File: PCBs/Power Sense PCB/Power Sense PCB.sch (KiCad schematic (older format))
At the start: 0 parts

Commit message: Complete Schematic
- Completed initial schematic
- Lots of test points
- Some footprints and BOM selected
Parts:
- added C1, C10, C11, C12, C2, C3, C4, C5, C6, C7, C8, C9: C_Small, Capacitors_SMD:C_0603, symbol Device:C_Small
- added H1, H2, H3, H4: MountingHole, Mounting_Holes:MountingHole_3mm_Pad_Via, symbol Mechanical:MountingHole
- added J1: Jack-DC, symbol Connector:Jack-DC
- added J2: PWR_INV, symbol Connector_Generic:Conn_01x02
- added J3: PWR_INPUT, symbol Connector_Generic:Conn_01x02
- added J4: PHASE_A_INV, symbol Connector_Generic:Conn_01x01
- added J5: PHASE_A_MOTOR, symbol Connector_Generic:Conn_01x01
- added J6: PHASE_B_INV, symbol Connector_Generic:Conn_01x01
- added J7: PHASE_B_MOTOR, symbol Connector_Generic:Conn_01x01
- added J8: PHASE_C_INV, symbol Connector_Generic:Conn_01x01
- added J9: PHASE_C_MOTOR, symbol Connector_Generic:Conn_01x01
- added NT1, NT2, NT3, NT4, NT5, NT6, NT7, NT8: Net-Tie_2, NetTies:NetTie-2_SMD_Pad0.5mm, symbol Device:Net-Tie_2
- added R1, R12, R13, R15, R2, R5, R6, R7: R_Small_US, Resistors_SMD:R_0603, symbol Device:R_Small_US
- added R10, R3, R4: 5m, symbol Device:R_US
- added R11, R8, R9: 10k, Resistors_SMD:R_0603, symbol Device:R_Small_US
- added R14: R_US, symbol Device:R_US
- added TP1: V_BUS, Testpoints:TestPoint_Loop_D1.80mm_Drill1.0mm_Beaded, symbol Connector:TestPoint
- added TP10, TP15, TP17, TP19, TP2, TP4, TP7, TP8: GND_REF, Testpoints:TestPoint_Loop_D1.80mm_Drill1.0mm_Beaded, symbol Connector:TestPoint
- added TP11, TP12, TP13: NEUTRAL_REF, Testpoints:TestPoint_Loop_D1.80mm_Drill1.0mm_Beaded, symbol Connector:TestPoint
- added TP14: I_PHASE_B, Testpoints:TestPoint_Loop_D1.80mm_Drill1.0mm_Beaded, symbol Connector:TestPoint
- added TP16: V_PHASE_C, Testpoints:TestPoint_Loop_D1.80mm_Drill1.0mm_Beaded, symbol Connector:TestPoint
- added TP18: I_PHASE_C, Testpoints:TestPoint_Loop_D1.80mm_Drill1.0mm_Beaded, symbol Connector:TestPoint
- added TP3: V_PHASE_A, Testpoints:TestPoint_Loop_D1.80mm_Drill1.0mm_Beaded, symbol Connector:TestPoint
- added TP5, TP6: I_PHASE_A, Testpoints:TestPoint_Loop_D1.80mm_Drill1.0mm_Beaded, symbol Connector:TestPoint
- added TP9: V_PHASE_B, Testpoints:TestPoint_Loop_D1.80mm_Drill1.0mm_Beaded, symbol Connector:TestPoint
- added U1, U2, U3, U4: INA240A1D, Housings_SOIC:SOIC-8-1EP_3.9x4.9mm_Pitch1.27mm, symbol Amplifier_Current:INA240A1D
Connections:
- new net: J2.1 (Pin_1), NT1.1, R1.2, R3.2
- new net: J3.1 (Pin_1), NT2.1, R3.1
- new net: J4.1 (Pin_1), NT3.1, R2.2, R4.2
- new net: C4.1, NT4.2, U2.8 (+)
- new net: C4.2, NT3.2, U2.1 (-)
- new net: R6.2, U2.5
- new net: J6.1 (Pin_1), NT5.1, R10.2, R7.2
- new net: C8.1, NT6.2, U3.8 (+)
- new net: C8.2, NT5.2, U3.1 (-)
- new net: R12.2, U3.5
- new net: J8.1 (Pin_1), NT7.1, R13.2, R14.2
- new net: C11.1, NT8.2, U4.8 (+)
- new net: C11.2, NT7.2, U4.1 (-)
- new net: R15.2, U4.5
- new net: C3.1, NT2.2, U1.8 (+)
- new net: C3.2, NT1.2, U1.1 (-)
- new net: R5.2, U1.5
- new net +5V: J1.1, U1.6 (V+), U1.7 (REF1), U2.6 (V+), U2.7 (REF1), U3.6 (V+), U3.7 (REF1), U4.6 (V+), U4.7 (REF1)
- new net GND: C1.2, C10.2, C12.2, C2.2, C5.2, C6.2, C7.2, C9.2, J1.2, J2.2 (Pin_2), J3.2 (Pin_2), TP10.1, TP15.1, TP17.1, TP19.1, TP2.1, TP4.1, TP7.1, TP8.1, U1.2 (GND), U1.3 (REF2), U1.4 (GND), U2.2 (GND), U2.3 (REF2), U2.4 (GND), U3.2 (GND), U3.3 (REF2), U3.4 (GND), U4.2 (GND), U4.3 (REF2), U4.4 (GND)
- new net I_BUS: C5.1, R5.1, TP5.1
- new net I_PHASE_A: C6.1, R6.1, TP6.1
- new net I_PHASE_B: C9.1, R12.1, TP14.1
- new net I_PHASE_C: C12.1, R15.1, TP18.1
- new net MOTOR_NEUTRAL: R11.1, R8.1, R9.1, TP11.1, TP12.1, TP13.1
- new net PHASE_A_MOTOR: J5.1 (Pin_1), NT4.1, R4.1, R8.2
- new net PHASE_B_MOTOR: J7.1 (Pin_1), NT6.1, R10.1, R9.2
- new net PHASE_C_MOTOR: J9.1 (Pin_1), NT8.1, R11.2, R14.1
- new net V_BUS: C1.1, R1.1, TP1.1
- new net V_PHASE_A: C2.1, R2.1, TP3.1
- new net V_PHASE_B: C7.1, R7.1, TP9.1
- new net V_PHASE_C: C10.1, R13.1, TP16.1
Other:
- note added: ""Fake" neutral star point"
- note added: "For RC LPFs, start with 1kHz corner freq, adjust later"
- note added: "See if 1000pF shunt cap helps\nfor current sense inputs"
- note added: "Should be approx the same\nvoltage as the real motor neutral, \nsince phases are close to balanced."

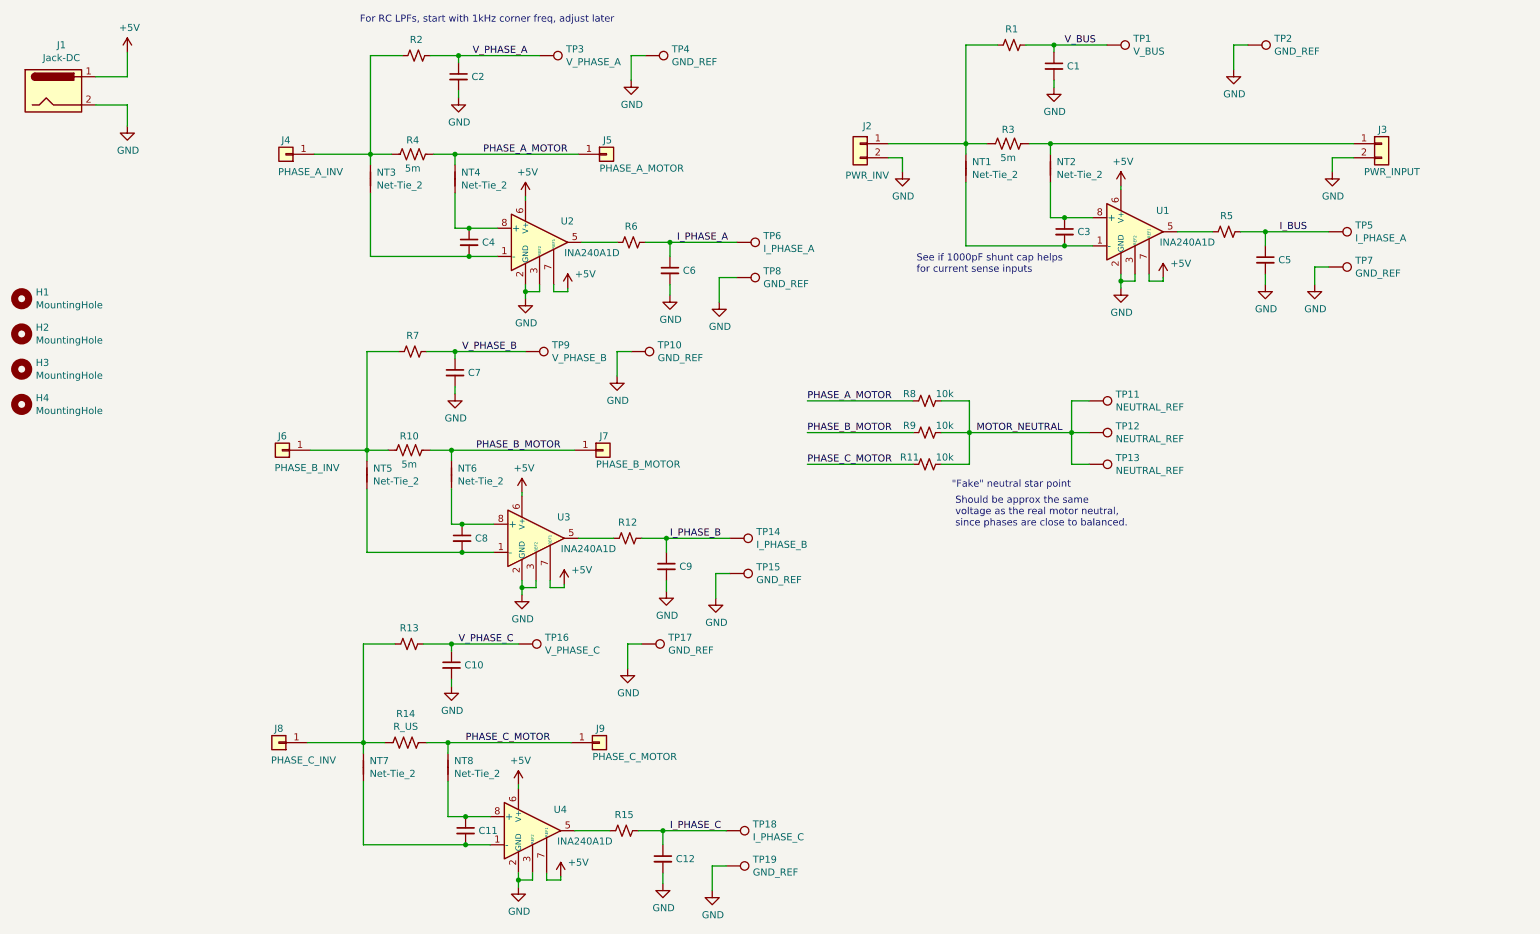
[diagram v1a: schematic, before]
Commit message: Schematic + BOM
- Added 0.1uF decoupling caps
- Added resistor division, same as DRV8305 eval board
- Spec'd more of the BOM
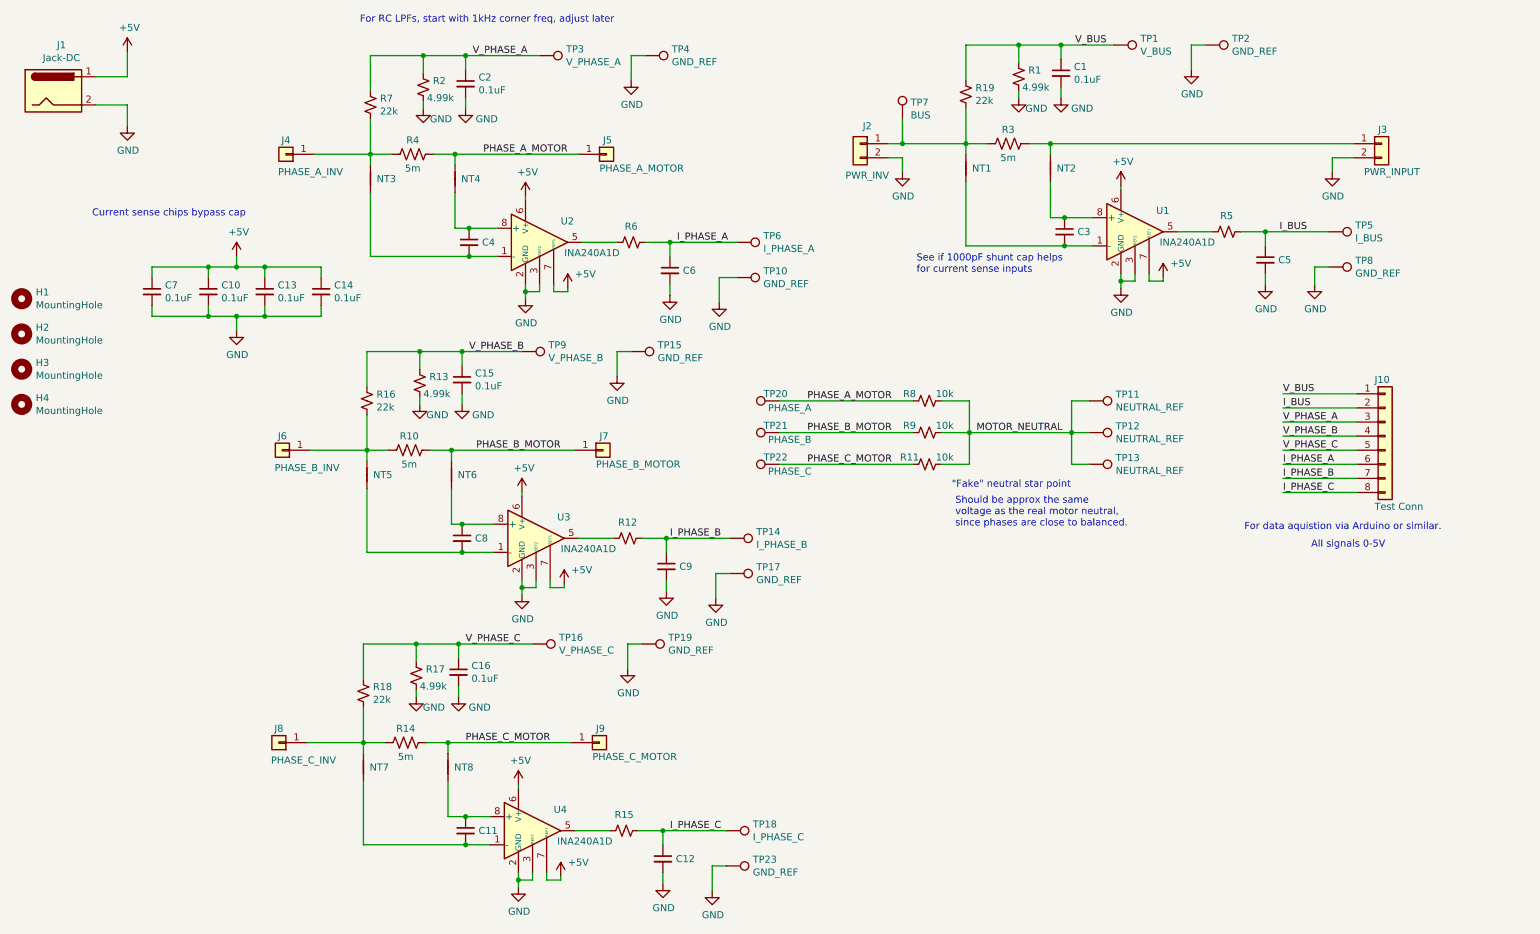
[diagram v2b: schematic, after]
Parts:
- added C13, C14, C15, C16: 0.1uF, Capacitors_SMD:C_0805, symbol Device:C_Small
- added J10: Test Conn, Pin_Headers:Pin_Header_Straight_1x08_Pitch2.54mm, symbol Connector_Generic:Conn_01x08
- added R16, R18, R19: 22k, Resistors_SMD:R_0603, symbol Device:R_Small_US
- added R17: 4.99k, Resistors_SMD:R_0603, symbol Device:R_Small_US
- added TP20: PHASE_A, Testpoints:TestPoint_Loop_D1.80mm_Drill1.0mm_Beaded, symbol Connector:TestPoint
- added TP21: PHASE_B, Testpoints:TestPoint_Loop_D1.80mm_Drill1.0mm_Beaded, symbol Connector:TestPoint
- added TP22: PHASE_C, Testpoints:TestPoint_Loop_D1.80mm_Drill1.0mm_Beaded, symbol Connector:TestPoint
- added TP23: GND_REF, Testpoints:TestPoint_Loop_D1.80mm_Drill1.0mm_Beaded, symbol Connector:TestPoint
- C1, C10, C2, C7: value C_Small -> 0.1uF; footprint Capacitors_SMD:C_0603 -> Capacitors_SMD:C_0805; Digikey (none) -> 478-12799-1-ND
- J1: footprint (none) -> Connectors:BARREL_JACK
- R1, R13, R2: value R_Small_US -> 4.99k
- R10, R3, R4: footprint (none) -> Power Sense PCB:R_2512_Sense; Digikey (none) -> YAG6124CT-ND
- R14: value R_US -> 5m; footprint (none) -> Power Sense PCB:R_2512_Sense; Digikey (none) -> YAG6124CT-ND
- R7: value R_Small_US -> 22k
- TP1, TP16, TP3, TP9: Digikey (none) -> 36-5117-ND
- TP10, TP11, TP12, TP13, TP15, TP17, TP19, TP2, TP4, TP8: Digikey (none) -> 36-5001-ND
- TP14, TP18, TP6: Digikey (none) -> 36-5119-ND
- TP5: value I_PHASE_A -> I_BUS; Digikey (none) -> 36-5119-ND
- TP7: value GND_REF -> BUS; Digikey (none) -> 36-5116-ND
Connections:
- net +5V: now also C10.1, C7.1, C13.1, C14.1
- net GND: now also R1.1, R13.1, R2.1, C13.2, C14.2, C15.2, C16.2, R17.1, TP23.1; no longer TP7.1
- net I_BUS: now also J10.2 (Pin_2)
- net I_PHASE_A: now also J10.6 (Pin_6)
- net I_PHASE_B: now also J10.7 (Pin_7)
- net I_PHASE_C: now also J10.8 (Pin_8)
- net PHASE_A_MOTOR: now also TP20.1
- net PHASE_B_MOTOR: now also TP21.1
- net PHASE_C_MOTOR: now also TP22.1
- net V_BUS: now also R1.2, J10.1 (Pin_1), R19.2; no longer R1.1
- net V_PHASE_A: now also R2.2, R7.2, J10.3 (Pin_3); no longer R2.1
- net V_PHASE_B: now also R13.2, C15.1, J10.4 (Pin_4), R16.2; no longer C7.1, R7.1
- net V_PHASE_C: now also C16.1, J10.5 (Pin_5), R17.2, R18.2; no longer C10.1, R13.1
- net at J2.1 (Pin_1), NT1.1, R3.2: now also TP7.1, R19.1; no longer R1.2
- net at J4.1 (Pin_1), NT3.1, R4.2: now also R7.1; no longer R2.2
- net at J6.1 (Pin_1), NT5.1, R10.2: now also R16.1; no longer R7.2
- net at J8.1 (Pin_1), NT7.1, R14.2: now also R18.1; no longer R13.2
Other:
- note added: "All signals 0-5V"
- note added: "Current sense chips bypass cap"
- note added: "For data aquistion via Arduino or similar."
- moved on the sheet: TP1, TP16, TP9

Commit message: BOM + Footprints
- BOM assigned
- Footprints assigned
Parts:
- J2, J3: footprint (none) -> Power Sense PCB:AMASS_XT60-M
- J4, J5, J6, J7, J8, J9: footprint (none) -> Power Sense PCB:3mm_Bullet_RA
- R1, R13, R17, R2: Digikey (none) -> P4.99KDBCT-ND
- R16, R18, R19, R7: Digikey (none) -> P22KDBCT-ND
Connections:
- net GND: now also J2.1 (Pin_1), J3.1 (Pin_1); no longer J2.2 (Pin_2), J3.2 (Pin_2)
- net at NT1.1, R19.1, R3.2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: now also J2.2 (Pin_2); no longer J2.1 (Pin_1)
- net at NT2.1, R3.1: now also J3.2 (Pin_2); no longer J3.1 (Pin_1)
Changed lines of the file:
@@
 L Connector_Generic:Conn_01x02 J2
 U 1 1 5E28B9A2
-P 6825 1625
-F 0 "J2" H 6775 1750 50  0000 C CNN
-F 1 "PWR_INV" H 6775 1400 50  0000 C CNN
-F 2 "" H 6825 1625 50  0001 C CNN
-F 3 "~" H 6825 1625 50  0001 C CNN
-	1    6825 1625
-	-1   0    0    -1
+P 6825 1725
+F 0 "J2" H 6775 1850 50  0000 C CNN
+F 1 "PWR_INV" H 6775 1500 50  0000 C CNN
+F 2 "Power Sense PCB:AMASS_XT60-M" H 6825 1725 50  0001 C CNN
+F 3 "~" H 6825 1725 50  0001 C CNN
+	1    6825 1725
+	-1   0    0    1
 $EndComp
 $Comp
 L Connector_Generic:Conn_01x02 J3
 U 1 1 5E28D757
-P 10525 1625
-F 0 "J3" H 10500 1725 50  0000 L CNN
-F 1 "PWR_INPUT" H 10400 1425 50  0000 L CNN
-F 2 "" H 10525 1625 50  0001 C CNN
-F 3 "~" H 10525 1625 50  0001 C CNN
-	1    10525 1625
-	1    0    0    -1
+P 10525 1725
+F 0 "J3" H 10500 1825 50  0000 L CNN
+F 1 "PWR_INPUT" H 10400 1525 50  0000 L CNN
+F 2 "Power Sense PCB:AMASS_XT60-M" H 10525 1725 50  0001 C CNN
+F 3 "~" H 10525 1725 50  0001 C CNN
+	1    10525 1725
+	1    0    0    1
 $EndComp
 $Comp
@@
 F 0 "J4" H 2750 1600 50  0000 C CNN
 F 1 "PHASE_A_INV" H 2575 1825 50  0000 C CNN
-F 2 "" H 2750 1700 50  0001 C CNN
+F 2 "Power Sense PCB:3mm_Bullet_RA" H 2750 1700 50  0001 C CNN
 F 3 "~" H 2750 1700 50  0001 C CNN
 	1    2750 1700
@@
 F 0 "J5" H 5000 1800 50  0000 L CNN
 F 1 "PHASE_A_MOTOR" H 4975 1600 50  0000 L CNN
-F 2 "" H 5025 1700 50  0001 C CNN
+F 2 "Power Sense PCB:3mm_Bullet_RA" H 5025 1700 50  0001 C CNN
 F 3 "~" H 5025 1700 50  0001 C CNN
 	1    5025 1700
@@
 F 0 "J6" H 2725 3700 50  0000 C CNN
 F 1 "PHASE_B_INV" H 2550 3925 50  0000 C CNN
-F 2 "" H 2725 3800 50  0001 C CNN
+F 2 "Power Sense PCB:3mm_Bullet_RA" H 2725 3800 50  0001 C CNN
 F 3 "~" H 2725 3800 50  0001 C CNN
 	1    2725 3800
@@
 F 0 "J7" H 4975 3900 50  0000 L CNN
 F 1 "PHASE_B_MOTOR" H 4950 3700 50  0000 L CNN
-F 2 "" H 5000 3800 50  0001 C CNN
+F 2 "Power Sense PCB:3mm_Bullet_RA" H 5000 3800 50  0001 C CNN
 F 3 "~" H 5000 3800 50  0001 C CNN
 	1    5000 3800
@@
 F 0 "J8" H 2700 5775 50  0000 C CNN
 F 1 "PHASE_C_INV" H 2525 6000 50  0000 C CNN
-F 2 "" H 2700 5875 50  0001 C CNN
+F 2 "Power Sense PCB:3mm_Bullet_RA" H 2700 5875 50  0001 C CNN
 F 3 "~" H 2700 5875 50  0001 C CNN
 	1    2700 5875
@@
 F 0 "J9" H 4950 5975 50  0000 L CNN
 F 1 "PHASE_C_MOTOR" H 4925 5775 50  0000 L CNN
-F 2 "" H 4975 5875 50  0001 C CNN
+F 2 "Power Sense PCB:3mm_Bullet_RA" H 4975 5875 50  0001 C CNN
 F 3 "~" H 4975 5875 50  0001 C CNN
 	1    4975 5875
@@
 F 2 "Resistors_SMD:R_0603" H 3350 1350 50  0001 C CNN
 F 3 "~" H 3350 1350 50  0001 C CNN
-F 4 "" H 3350 1350 50  0001 C CNN "Digikey"
+F 4 "P22KDBCT-ND" H 3350 1350 50  0001 C CNN "Digikey"
 	1    3350 1350
 	-1   0    0    1
@@
 F 2 "Resistors_SMD:R_0603" H 3725 1225 50  0001 C CNN
 F 3 "~" H 3725 1225 50  0001 C CNN
-F 4 "" H 3725 1225 50  0001 C CNN "Digikey"
+F 4 "P4.99KDBCT-ND" H 3725 1225 50  0001 C CNN "Digikey"
 	1    3725 1225
 	-1   0    0    1
@@
 F 2 "Resistors_SMD:R_0603" H 3700 3325 50  0001 C CNN
 F 3 "~" H 3700 3325 50  0001 C CNN
-F 4 "" H 3700 3325 50  0001 C CNN "Digikey"
+F 4 "P4.99KDBCT-ND" H 3700 3325 50  0001 C CNN "Digikey"
 	1    3700 3325
 	-1   0    0    1
@@
 F 2 "Resistors_SMD:R_0603" H 3325 3450 50  0001 C CNN
 F 3 "~" H 3325 3450 50  0001 C CNN
-F 4 "" H 3325 3450 50  0001 C CNN "Digikey"
+F 4 "P22KDBCT-ND" H 3325 3450 50  0001 C CNN "Digikey"
 	1    3325 3450
 	-1   0    0    1
@@
 F 2 "Resistors_SMD:R_0603" H 3300 5525 50  0001 C CNN
 F 3 "~" H 3300 5525 50  0001 C CNN
-F 4 "" H 3300 5525 50  0001 C CNN "Digikey"
+F 4 "P22KDBCT-ND" H 3300 5525 50  0001 C CNN "Digikey"
 	1    3300 5525
 	-1   0    0    1
@@
 F 2 "Resistors_SMD:R_0603" H 3675 5400 50  0001 C CNN
 F 3 "~" H 3675 5400 50  0001 C CNN
-F 4 "" H 3675 5400 50  0001 C CNN "Digikey"
+F 4 "P4.99KDBCT-ND" H 3675 5400 50  0001 C CNN "Digikey"
 	1    3675 5400
 	-1   0    0    1
@@
 F 2 "Resistors_SMD:R_0603" H 7575 1275 50  0001 C CNN
 F 3 "~" H 7575 1275 50  0001 C CNN
-F 4 "" H 7575 1275 50  0001 C CNN "Digikey"
+F 4 "P22KDBCT-ND" H 7575 1275 50  0001 C CNN "Digikey"
 	1    7575 1275
 	-1   0    0    1
@@
 F 2 "Resistors_SMD:R_0603" H 7950 1150 50  0001 C CNN
 F 3 "~" H 7950 1150 50  0001 C CNN
-F 4 "" H 7950 1150 50  0001 C CNN "Digikey"
+F 4 "P4.99KDBCT-ND" H 7950 1150 50  0001 C CNN "Digikey"
 	1    7950 1150
 	-1   0    0    1
